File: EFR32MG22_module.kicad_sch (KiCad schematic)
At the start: 34 parts, among them J1 USB_B_Micro 10118194-0011LF, J2 Conn_01x10, J3 Conn_ARM_JTAG_SWD_10, J4 Conn_01x10, U1 EFR32MG22C224F512GN32, U2 TLV75533PDBV, Y1 Crystal ECS-384-CDX-1983-TR3

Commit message: final commit? (?)
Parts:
- J3: value Conn_ARM_JTAG_SWD_10 -> ARM_2x5; footprint ARM_DEBUG:CNC_Tech_2x5_ARM_DEBUG -> arm_2x5:322010030000TR
- L3: footprint Inductor_SMD:L_0603_1608Metric_Pad1.05x0.95mm_HandSolder -> Inductor_SMD:L_0805_2012Metric_Pad1.15x1.40mm_HandSolder
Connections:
- net GND: now also J4.10 (Pin_10); no longer J4.9 (Pin_9)
- net RESET_N: now also J4.9 (Pin_9); no longer J4.10 (Pin_10)
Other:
- moved on the sheet: C14, C15, C16, C17, FB1, FB2

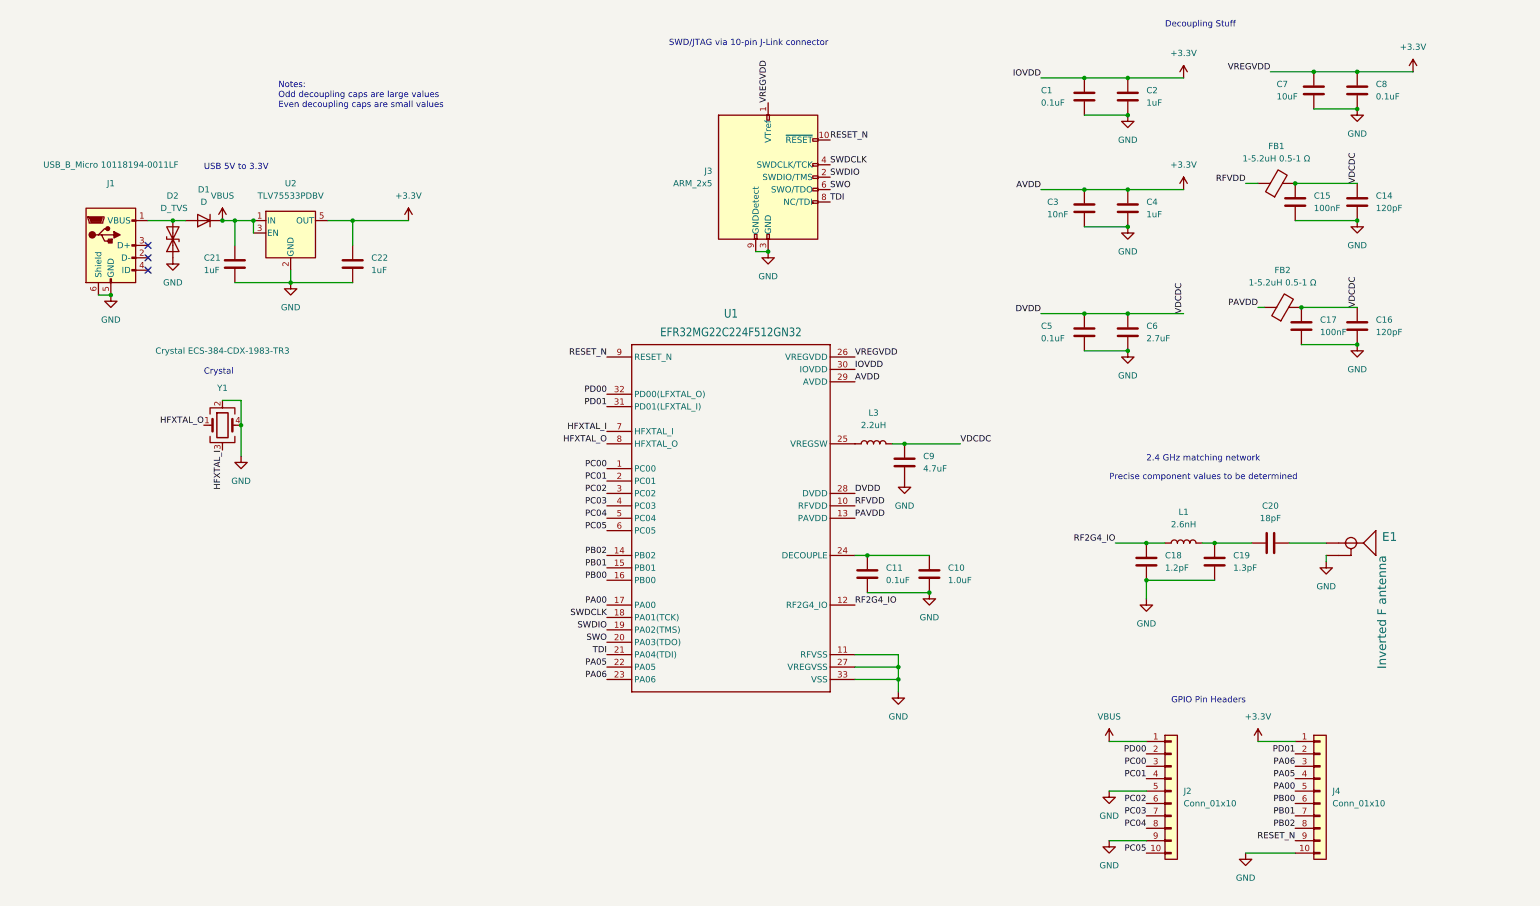
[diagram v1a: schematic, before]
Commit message: first pass at layout and routing for second revision
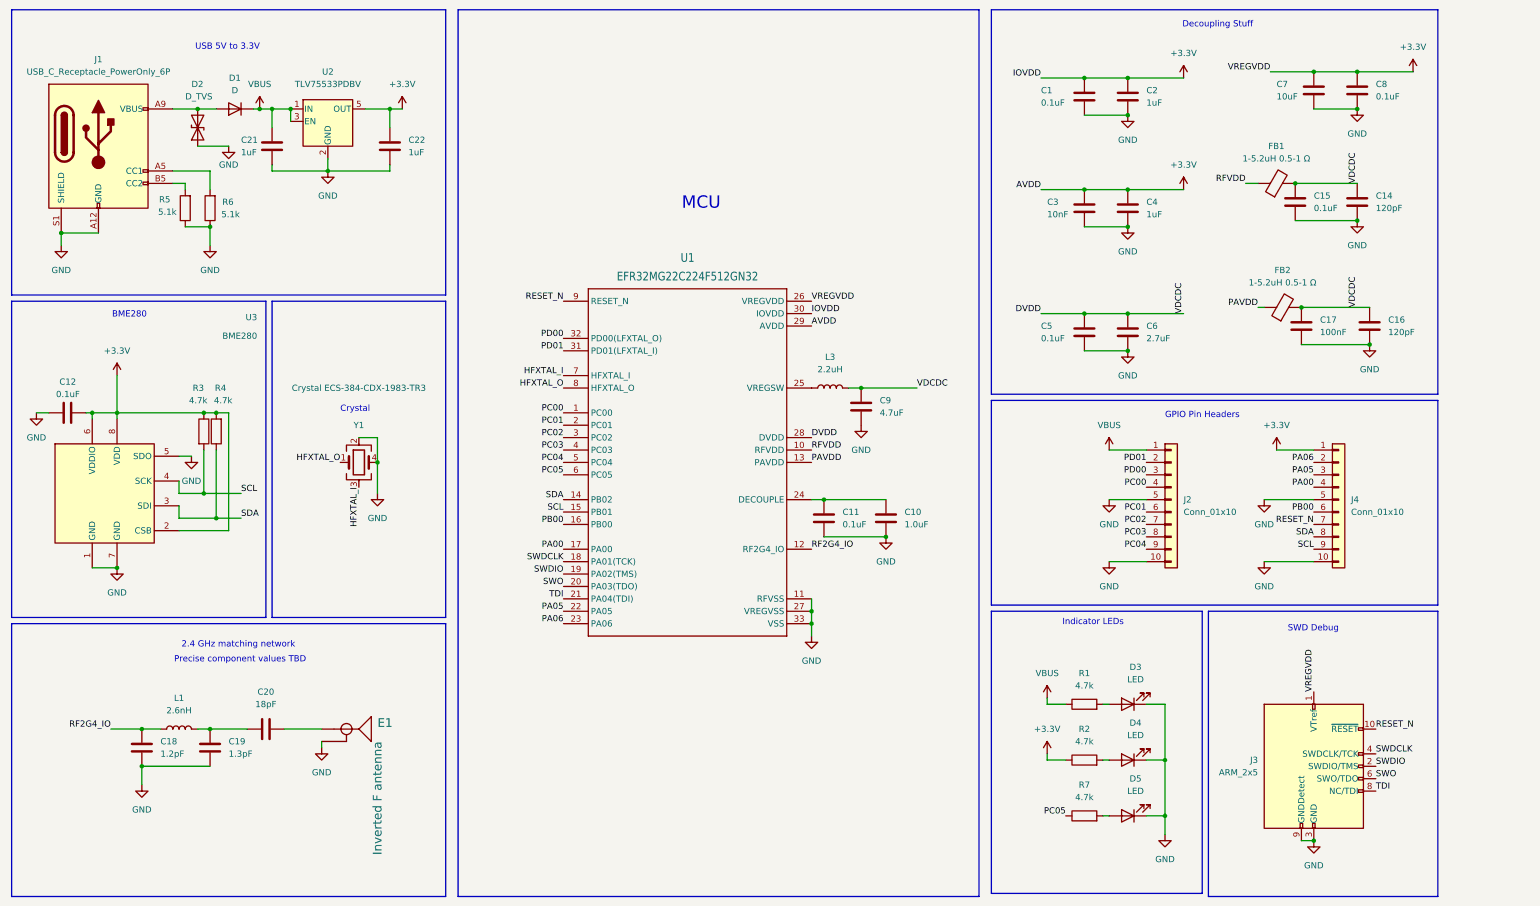
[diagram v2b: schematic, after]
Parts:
- removed J1: USB_B_Micro 10118194-0011LF, Connector_USB:USB_Micro-B_Amphenol_10118194_Horizontal, symbol Connector:USB_B_Micro
- added C12: 0.1uF, Capacitor_SMD:C_0402_1005Metric_Pad0.74x0.62mm_HandSolder, symbol Device:C
- added D3, D4, D5: LED, Diode_SMD:D_0603_1608Metric_Pad1.05x0.95mm_HandSolder, symbol Device:LED
- added J1: USB_C_Receptacle_PowerOnly_6P, Connector_USB:USB_C_Receptacle_GCT_USB4125-xx-x-0190_6P_TopMnt_Horizontal, symbol Connector:USB_C_Receptacle_PowerOnly_6P
- added R1, R2, R3, R4, R7: 4.7k, Resistor_SMD:R_0402_1005Metric_Pad0.72x0.64mm_HandSolder, symbol Device:R
- added R5, R6: 5.1k, Resistor_SMD:R_0402_1005Metric_Pad0.72x0.64mm_HandSolder, symbol Device:R
- added U3: BME280, Package_LGA:Bosch_LGA-8_2.5x2.5mm_P0.65mm_ClockwisePinNumbering, symbol Sensor:BME280
- C1, C10, C11, C14, C16, C17, C18, C19, C2, C20, C21, C22, C3, C4, C5, C6, C7, C8, C9: footprint Capacitor_SMD:C_0603_1608Metric_Pad1.08x0.95mm_HandSolder -> Capacitor_SMD:C_0402_1005Metric_Pad0.74x0.62mm_HandSolder
- C15: value 100nF -> 0.1uF; footprint Capacitor_SMD:C_0603_1608Metric_Pad1.08x0.95mm_HandSolder -> Capacitor_SMD:C_0402_1005Metric_Pad0.74x0.62mm_HandSolder
- J3: footprint arm_2x5:322010030000TR -> ARM_DEBUG:CNC_Tech_2x5_ARM_DEBUG
- L1: footprint Inductor_SMD:L_0603_1608Metric_Pad1.05x0.95mm_HandSolder -> Inductor_SMD:L_0402_1005Metric_Pad0.77x0.64mm_HandSolder
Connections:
- net +3.3V: now also C12.2, R2.1, R3.1, R4.2, U3.2 (CSB), U3.6 (VDDIO), U3.8 (VDD)
- net GND: now also J2.10 (Pin_10), J4.5 (Pin_5), C12.1, D3.1 (K), D4.1 (K), D5.1 (K), J1.A12 (GND), J1.B12 (GND), J1.S1 (SHIELD), R5.1, R6.1, U3.1 (GND), U3.5 (SDO), U3.7 (GND); no longer J2.9 (Pin_9)
- net PA00: now also J4.4 (Pin_4); no longer J4.5 (Pin_5)
- net PA05: now also J4.3 (Pin_3); no longer J4.4 (Pin_4)
- net PA06: now also J4.2 (Pin_2); no longer J4.3 (Pin_3)
- net PC00: now also J2.4 (Pin_4); no longer J2.3 (Pin_3)
- net PC01: now also J2.6 (Pin_6); no longer J2.4 (Pin_4)
- net PC02: now also J2.7 (Pin_7); no longer J2.6 (Pin_6)
- net PC03: now also J2.8 (Pin_8); no longer J2.7 (Pin_7)
- net PC04: now also J2.9 (Pin_9); no longer J2.8 (Pin_8)
- net PC05: now also R7.1; no longer J2.10 (Pin_10)
- net PD00: now also J2.3 (Pin_3); no longer J2.2 (Pin_2)
- net PD01: now also J2.2 (Pin_2); no longer J4.2 (Pin_2)
- net RESET_N: now also J4.7 (Pin_7); no longer J4.9 (Pin_9)
- net VBUS: now also R1.1
- net at D1.2 (A), D2.2 (A2): now also J1.A9 (VBUS), J1.B9 (VBUS)
- net PB01 renamed SCL
- net SCL: now also J4.9 (Pin_9), R3.2, U3.4 (SCK); no longer J4.7 (Pin_7)
- net PB02 renamed SDA
- net SDA: now also R4.1, U3.3 (SDI)
- new net: D5.2 (A), R7.2
- new net: J1.B5 (CC2), R5.2
- new net: D3.2 (A), R1.2
- new net: D4.2 (A), R2.2
- new net: J1.A5 (CC1), R6.2
- no-connect marks 3 -> 0
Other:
- note added: "BME280"
- note added: "Indicator LEDs"
- note added: "MCU"
- note added: "Precise component values TBD"
- note added: "SWD Debug"
- note removed: "Notes: Odd decoupling caps are large values Even decoupling caps are small values"
- note removed: "Precise component values to be determined"
- note removed: "SWD/JTAG via 10-pin J-Link connector"
- moved on the sheet: C10, C11, C16, C18, C19, C20, C21, C22, C9, D1, D2, E1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

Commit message: minor tweaks for component selection
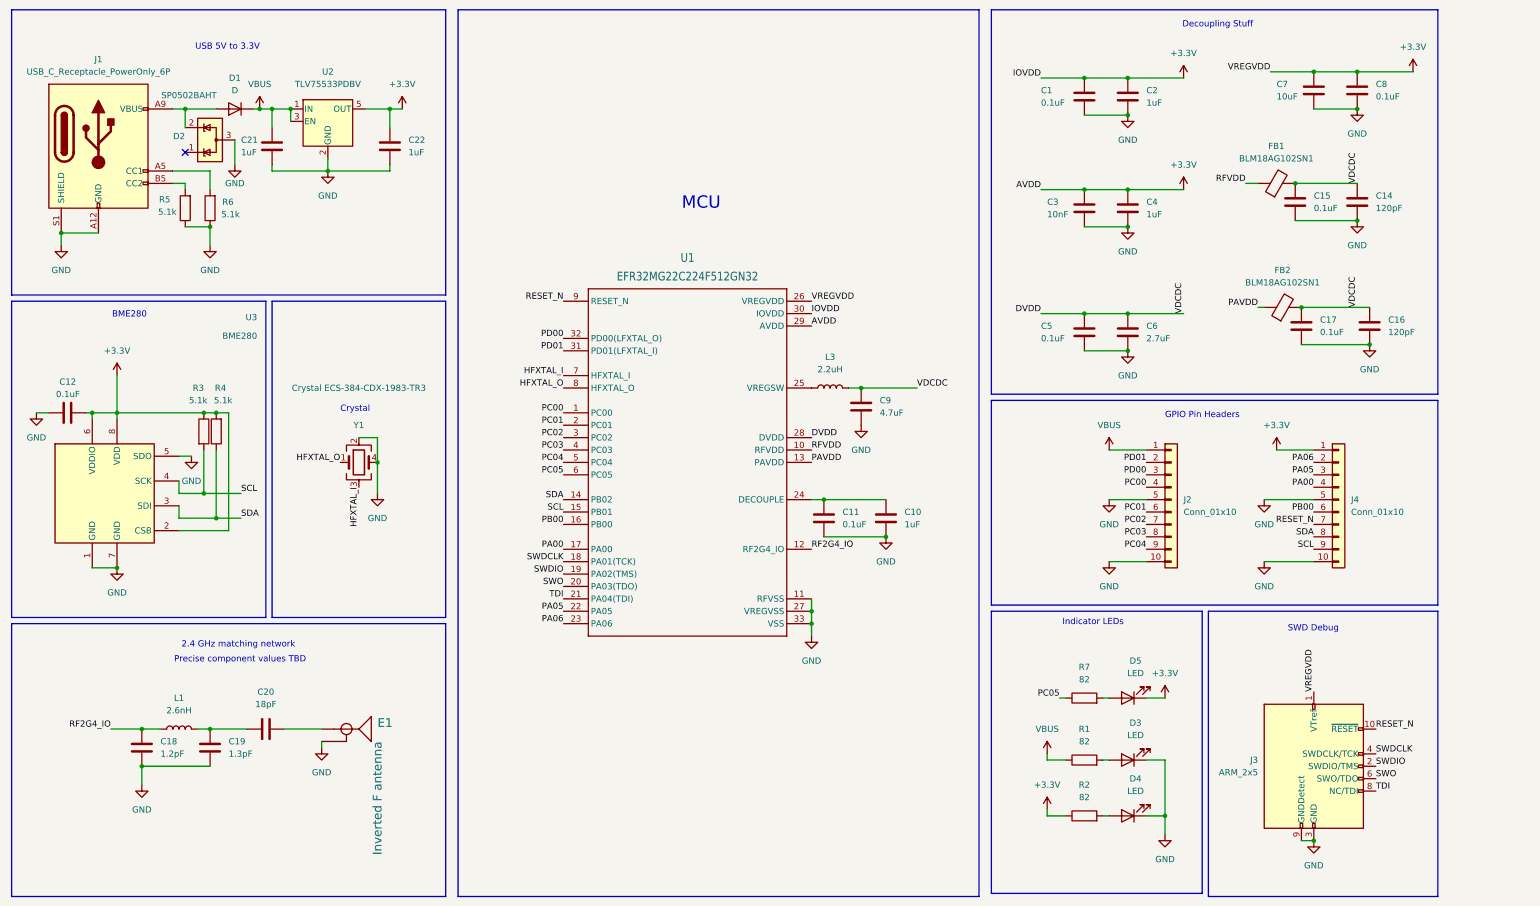
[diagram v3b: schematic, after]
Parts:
- removed D2: D_TVS, Diode_SMD:D_0201_0603Metric, symbol Device:D_TVS
- added D2: SP0502BAHT, Package_TO_SOT_SMD:SOT-23, symbol Power_Protection:SP0502BAHT
- C10: value 1.0uF -> 1uF
- C17: value 100nF -> 0.1uF
- C6, C7, C9: footprint Capacitor_SMD:C_0402_1005Metric_Pad0.74x0.62mm_HandSolder -> Capacitor_SMD:C_0603_1608Metric_Pad1.08x0.95mm_HandSolder
- FB1, FB2: value 1-5.2uH 0.5-1 Ω -> BLM18AG102SN1
- R1, R2, R7: value 4.7k -> 82
- R3, R4: value 4.7k -> 5.1k
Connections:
- net +3.3V: now also D5.1 (K)
- net GND: now also D2.3 (A); no longer D5.1 (K)
- net at D1.2 (A), J1.A9 (VBUS), J1.B9 (VBUS): now also D2.2 (K)
- no-connect marks 0 -> 1
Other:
- moved on the sheet: D3, D4, R1, R2

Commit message: silkscreen
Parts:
- R1: value 82 -> 220
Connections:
- net +3.3V: now also D5.2 (A); no longer D5.1 (K)
- net at R7.2: now also D5.1 (K); no longer D5.2 (A)
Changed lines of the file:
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@@
 			)
 		)
-		(property "Value" "82"
+		(property "Value" "220"
 			(at 222.25 153.67 90)
 			(effects
@@
 	)
 	(symbol
-		(lib_id "Device:LED")
-		(at 231.14 144.78 180)
-		(unit 1)
-		(exclude_from_sim no)
-		(in_bom yes)
-		(on_board yes)
-		(dnp no)
-		(fields_autoplaced yes)
-		(property "Reference" "D5"
-			(at 232.7275 137.16 0)
-			(effects
-				(font
-					(size 1.27 1.27)
-				)
-			)
-		)
-		(property "Value" "LED"
-			(at 232.7275 139.7 0)
-			(effects
-				(font
-					(size 1.27 1.27)
-				)
-			)
-		)
-		(property "Footprint" "Diode_SMD:D_0603_1608Metric_Pad1.05x0.95mm_HandSolder"
-			(at 231.14 144.78 0)
-			(effects
-				(font
-					(size 1.27 1.27)
-				)
-				(hide yes)
-			)
-		)
-		(property "Datasheet" "~"
-			(at 231.14 144.78 0)
-			(effects
-				(font
-					(size 1.27 1.27)
-				)
-				(hide yes)
-			)
-		)
-		(property "Description" "Light emitting diode"
-			(at 231.14 144.78 0)
-			(effects
-				(font
-					(size 1.27 1.27)
-				)
-				(hide yes)
-			)
-		)
-		(pin "2"
-		)
-		(pin "1"
-		)
-		(instances
-			(project "EFR32MG22_module"
-				(path "/2b6fdb38-3ff0-474e-9918-afa124d18892"
-					(reference "D5")
-					(unit 1)
-				)
-			)
-		)
-	)
-	(symbol
 		(lib_id "Device:L")
 		(at 170.18 81.28 90)
@@
 					(unit 1)
 				)
+			)
+		)
+	)
+	(symbol
+		(lib_id "Device:LED")
+		(at 231.14 144.78 0)
+		(unit 1)
+		(exclude_from_sim no)
+		(in_bom yes)
+		(on_board yes)
+		(dnp no)
+		(property "Reference" "D5"
+			(at 231.14 138.43 0)
+			(effects
+				(font
+					(size 1.27 1.27)
+				)
+			)
+		)
+		(property "Value" "LED"
+			(at 231.14 140.97 0)
+			(effects
+				(font
+					(size 1.27 1.27)
+				)
+			)
+		)
+		(property "Footprint" "Diode_SMD:D_0603_1608Metric_Pad1.05x0.95mm_HandSolder"
+			(at 231.14 144.78 0)
+			(effects
+				(font
+					(size 1.27 1.27)
+				)
+				(hide yes)
+			)
+		)
+		(property "Datasheet" "~"
+			(at 231.14 144.78 0)
+			(effects
+				(font
+					(size 1.27 1.27)
+				)
+				(hide yes)
+			)
+		)
+		(property "Description" "Light emitting diode"
+			(at 231.14 144.78 0)
+			(effects
+				(font
+					(size 1.27 1.27)
+				)
+				(hide yes)
+			)
+		)
+		(pin "2"
+		)
+		(pin "1"
+		)
+		(instances
+			(project "EFR32MG22_module"
+				(path "/2b6fdb38-3ff0-474e-9918-afa124d18892"
+					(reference "D5")
+					(unit 1)
+				)
